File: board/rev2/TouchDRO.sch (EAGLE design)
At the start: 26 parts, among them U2 VREG_33, U3 VREG_5

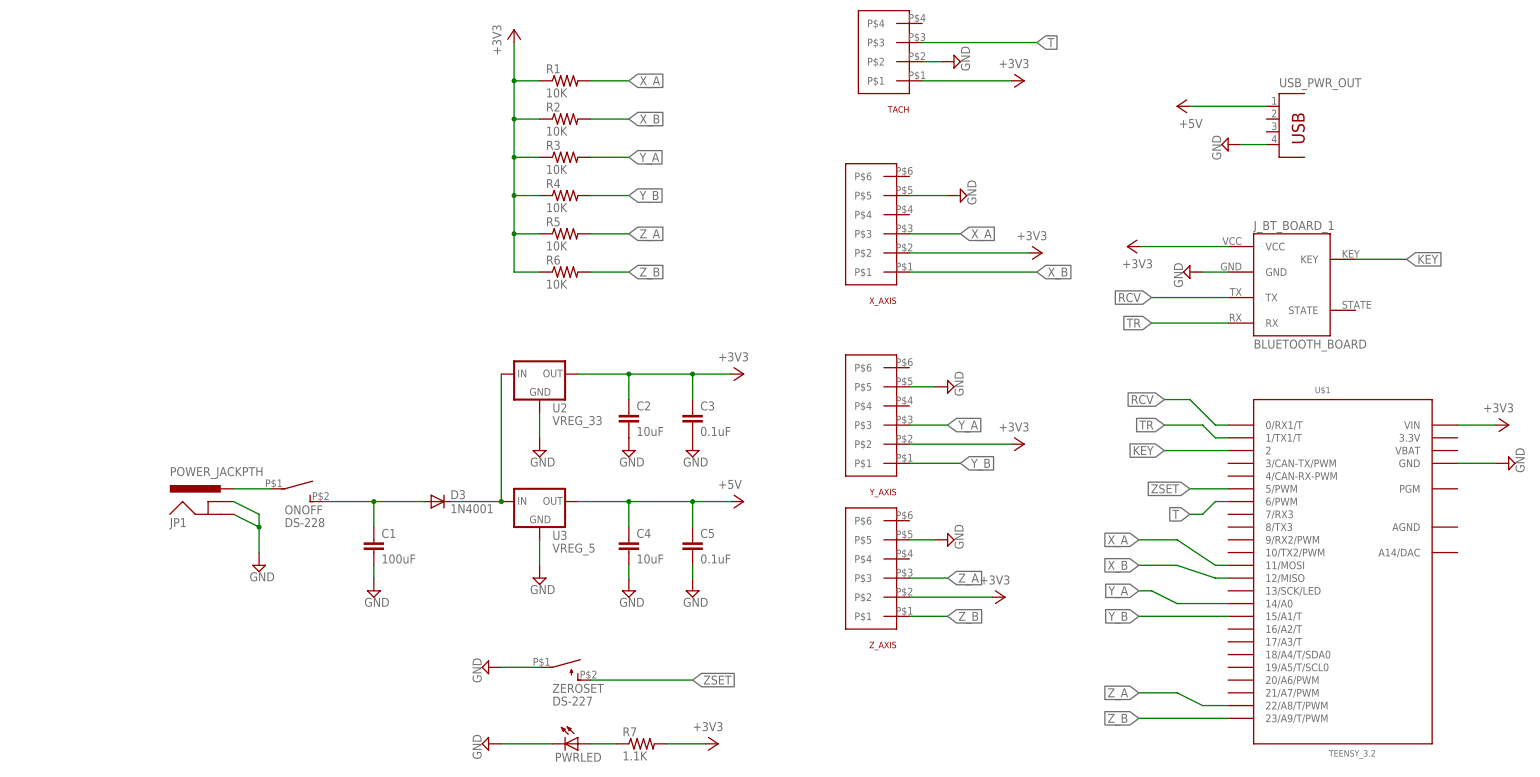
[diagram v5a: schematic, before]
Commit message: renamed connectors library. update regulators to have PWR signal pin. added Vcc resistor to support sherline encoder. updated TouchDRO sketch to use the new button and frequency libraries, disable bluetooth name set functionality
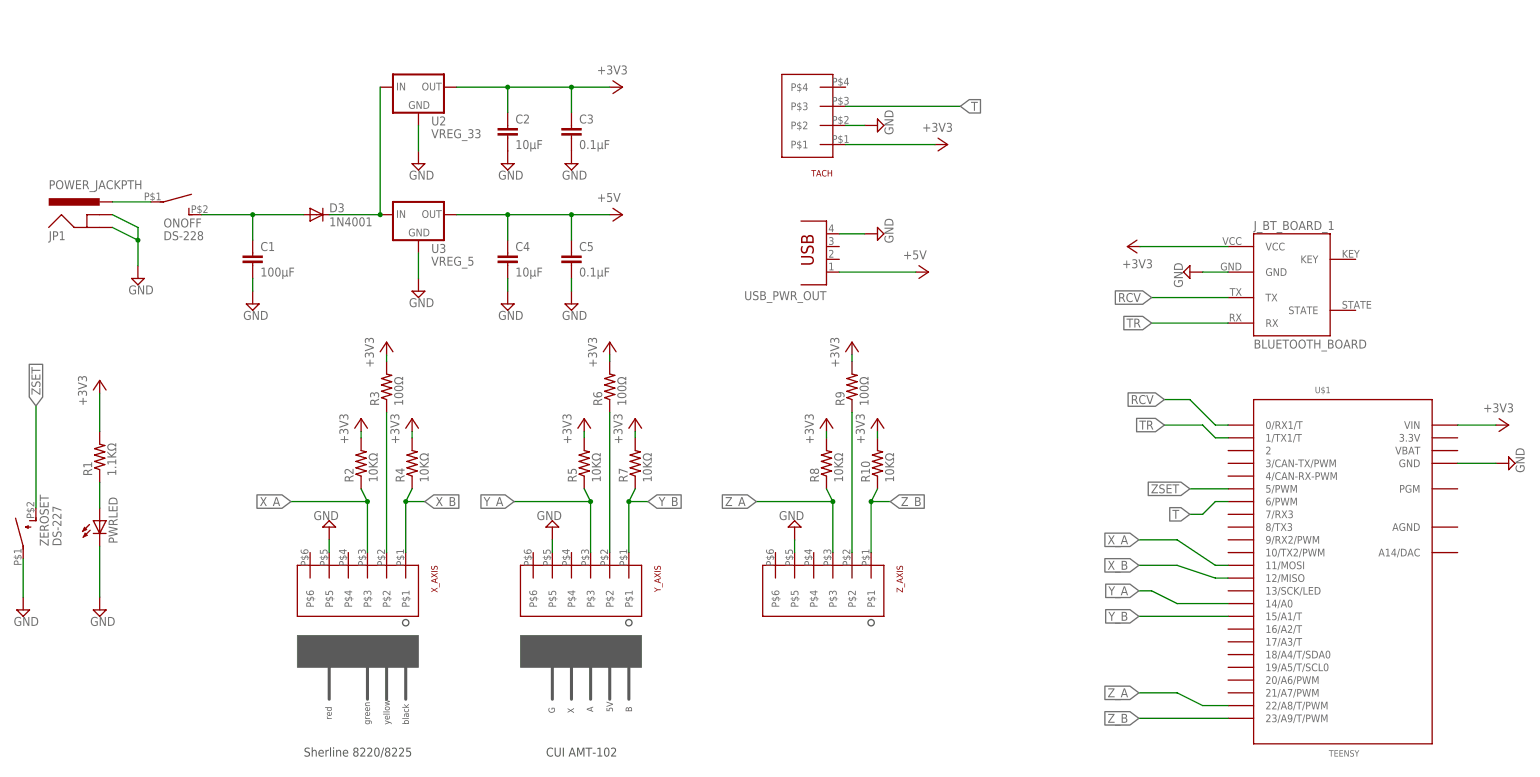
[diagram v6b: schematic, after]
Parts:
- added R10, R8: 10KΩ, SparkFun-Passives:RESISTOREZ
- added R9: 100Ω, SparkFun-Passives:RESISTOREZ
- C1: value 100uF -> 100µF
- C2, C4: value 10uF -> 10µF
- C3, C5: value 0.1uF -> 0.1µF
- R1: value 10K -> 1.1KΩ
- R2, R4, R5: value 10K -> 10KΩ
- R3, R6: value 10K -> 100Ω
- R7: value 1.1K -> 10KΩ
- U$1: value TEENSY_3.2 -> TEENSY
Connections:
- removed net KEY: J_BT_BOARD_1.KEY, U$1.2
- new net N$3: R9.1, Z_AXIS.P$2
- new net N$5: R6.1, Y_AXIS.P$2
- new net N$7: R3.1, X_AXIS.P$2
- net +3V3: now also R1.2, R10.2, R2.2, R3.2, R4.2, R5.2, R6.2, R8.2, R9.2; no longer R1.1, R2.1, R3.1, R4.1, R5.1, R6.1, X_AXIS.P$2, Y_AXIS.P$2, Z_AXIS.P$2
- net N$1: now also R1.1; no longer R7.1
- net X_A: now also R2.1; no longer R1.2
- net X_B: now also R4.1; no longer R2.2
- net Y_A: now also R5.1; no longer R3.2
- net Y_B: now also R7.1; no longer R4.2
- net Z_A: now also R8.1; no longer R5.2
- net Z_B: now also R10.1; no longer R6.2
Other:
- note added: "5V"
- note added: "A"
- note added: "B"
- note added: "CUI AMT-102"
- note added: "G"
- note added: "Sherline 8220/8225"
- note added: "X"
- note added: "black"
- note added: "green"
- note added: "red"
- note added: "yellow"
- moved on the sheet: C1, C2, C3, C4, C5, D3, JP1, ONOFF, PWRLED, R1, R2, R3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

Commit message: cleaned up connector components. updated images
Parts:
- renumbered U2 to VREG33, U3 to VREG50
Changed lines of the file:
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@@
 <setting verticaltext="up"/>
 </settings>
-<grid distance="0.05" unitdist="inch" unit="inch" style="lines" multiple="1" display="no" altdistance="0.025" altunitdist="inch" altunit="inch"/>
+<grid distance="0.1" unitdist="inch" unit="inch" style="lines" multiple="1" display="no" altdistance="0.01" altunitdist="inch" altunit="inch"/>
 <layers>
 <layer number="1" name="Top" color="4" fill="1" visible="no" active="no"/>
@@
 <part name="ZEROSET" library="Switches" deviceset="DS-227" device=""/>
 <part name="ONOFF" library="Switches" deviceset="DS-228" device=""/>
-<part name="U2" library="regulators" deviceset="VREG_33" device=""/>
-<part name="U3" library="regulators" deviceset="VREG_5" device=""/>
+<part name="VREG33" library="regulators" deviceset="VREG_33" device="" value="VREG_33"/>
+<part name="VREG50" library="regulators" deviceset="VREG_5" device="" value="VREG_5"/>
 <part name="PWRLED" library="led" deviceset="LED" device="3MM"/>
 <part name="SUPPLY4" library="supply2" deviceset="GND" device=""/>
@@
 <instance part="ZEROSET" gate="G$1" x="-184.15" y="-11.43"/>
 <instance part="ONOFF" gate="G$1" x="-153.67" y="54.61" rot="R270"/>
-<instance part="U2" gate="G$1" x="-105.41" y="77.47"/>
-<instance part="U3" gate="G$1" x="-105.41" y="52.07"/>
+<instance part="VREG33" gate="G$1" x="-105.41" y="77.47"/>
+<instance part="VREG50" gate="G$1" x="-105.41" y="52.07"/>
 <instance part="PWRLED" gate="G$1" x="-168.91" y="-8.89"/>
 <instance part="SUPPLY4" gate="GND" x="-168.91" y="-26.67"/>
@@
 <pinref part="SUPPLY15" gate="GND" pin="GND"/>
 <wire x1="-105.41" y1="69.85" x2="-105.41" y2="64.77" width="0.1524" layer="91"/>
-<pinref part="U2" gate="G$1" pin="GND"/>
+<pinref part="VREG33" gate="G$1" pin="GND"/>
 </segment>
 <segment>
 <pinref part="SUPPLY18" gate="GND" pin="GND"/>
 <wire x1="-105.41" y1="39.37" x2="-105.41" y2="44.45" width="0.1524" layer="91"/>
-<pinref part="U3" gate="G$1" pin="GND"/>
+<pinref part="VREG50" gate="G$1" pin="GND"/>
 </segment>
 <segment>
@@
 <wire x1="-74.93" y1="52.07" x2="-67.31" y2="52.07" width="0.1524" layer="91"/>
 <wire x1="-87.63" y1="52.07" x2="-87.63" y2="46.99" width="0.1524" layer="91"/>
-<pinref part="U3" gate="G$1" pin="OUT"/>
+<pinref part="VREG50" gate="G$1" pin="OUT"/>
 <pinref part="C5" gate="G$1" pin="1"/>
 <wire x1="-74.93" y1="46.99" x2="-74.93" y2="52.07" width="0.1524" layer="91"/>
@@
 <wire x1="-74.93" y1="77.47" x2="-67.31" y2="77.47" width="0.1524" layer="91"/>
 <wire x1="-87.63" y1="77.47" x2="-87.63" y2="72.39" width="0.1524" layer="91"/>
-<pinref part="U2" gate="G$1" pin="OUT"/>
+<pinref part="VREG33" gate="G$1" pin="OUT"/>
 <pinref part="C3" gate="G$1" pin="1"/>
 <wire x1="-74.93" y1="72.39" x2="-74.93" y2="77.47" width="0.1524" layer="91"/>
@@
 <wire x1="-123.19" y1="52.07" x2="-113.03" y2="52.07" width="0.1524" layer="91"/>
 <junction x="-113.03" y="52.07"/>
-<pinref part="U2" gate="G$1" pin="IN"/>
-<pinref part="U3" gate="G$1" pin="IN"/>
-</segment>
-</net>
+<pinref part="VREG33" gate="G$1" pin="IN"/>
+<pinref part="VREG50" gate="G$1" pin="IN"/>
+</segment>
+</net>

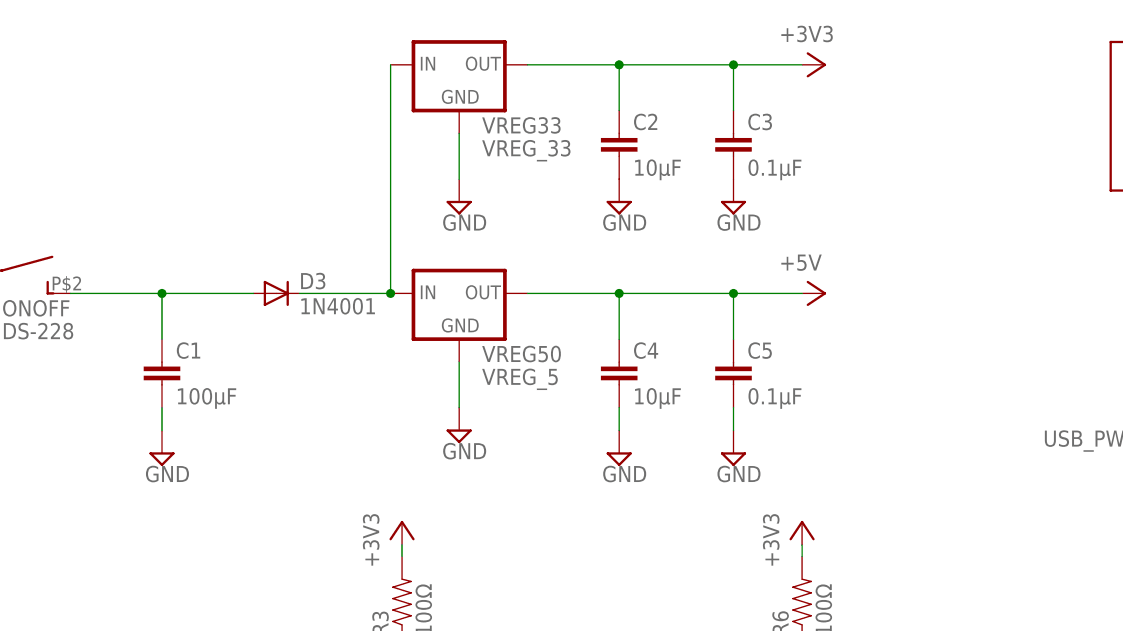
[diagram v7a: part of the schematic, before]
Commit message: adding latest pcb layout 3d model. finalized rev2 wiring, specifically wider routes on GND and VCC
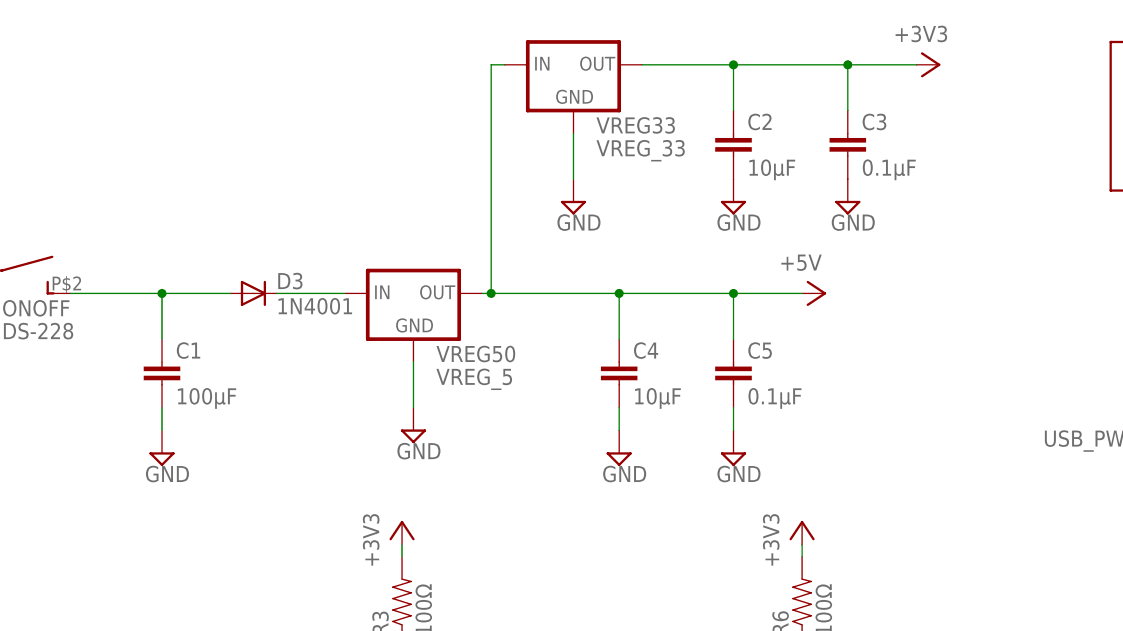
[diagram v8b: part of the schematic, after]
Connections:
- net +5V: now also VREG33.IN
- net D1: no longer VREG33.IN
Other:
- moved on the sheet: C2, C3, D3, VREG33, VREG50
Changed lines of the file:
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@@
 <instance part="SUPPLY10" gate="GND" x="-13.97" y="69.85" rot="R90"/>
 <instance part="SUPPLY11" gate="GND" x="48.26" y="40.64" rot="R270"/>
-<instance part="D3" gate="G$1" x="-125.73" y="52.07"/>
+<instance part="D3" gate="G$1" x="-128.27" y="52.07"/>
 <instance part="C4" gate="G$1" x="-87.63" y="41.91"/>
 <instance part="JP1" gate="G$1" x="-168.91" y="46.99"/>
 <instance part="SUPPLY13" gate="GND" x="-161.29" y="39.37"/>
-<instance part="SUPPLY15" gate="GND" x="-105.41" y="62.23"/>
+<instance part="SUPPLY15" gate="GND" x="-92.71" y="62.23"/>
 <instance part="SUPPLY16" gate="GND" x="-87.63" y="34.29"/>
-<instance part="SUPPLY18" gate="GND" x="-105.41" y="36.83"/>
+<instance part="SUPPLY18" gate="GND" x="-110.49" y="36.83"/>
 <instance part="SUPPLY20" gate="GND" x="-13.97" y="48.26" rot="R90"/>
 <instance part="P+2" gate="1" x="-64.77" y="52.07" rot="R270"/>
-<instance part="+3V3" gate="G$1" x="-64.77" y="77.47" rot="R270"/>
+<instance part="+3V3" gate="G$1" x="-52.07" y="77.47" rot="R270"/>
 <instance part="+3V4" gate="G$1" x="111.76" y="10.16" rot="R270"/>
 <instance part="+3V6" gate="G$1" x="0" y="66.04" rot="R270"/>
-<instance part="C2" gate="G$1" x="-87.63" y="67.31"/>
-<instance part="SUPPLY1" gate="GND" x="-87.63" y="62.23"/>
+<instance part="C2" gate="G$1" x="-74.93" y="67.31"/>
+<instance part="SUPPLY1" gate="GND" x="-74.93" y="62.23"/>
 <instance part="+3V1" gate="G$1" x="35.814" y="45.72" rot="R90"/>
 <instance part="P+1" gate="1" x="-3.81" y="40.64" rot="R270"/>
@@
 <instance part="ZEROSET" gate="G$1" x="-184.15" y="-11.43"/>
 <instance part="ONOFF" gate="G$1" x="-153.67" y="54.61" rot="R270"/>
-<instance part="VREG33" gate="G$1" x="-105.41" y="77.47"/>
-<instance part="VREG50" gate="G$1" x="-105.41" y="52.07"/>
+<instance part="VREG33" gate="G$1" x="-92.71" y="77.47"/>
+<instance part="VREG50" gate="G$1" x="-110.49" y="52.07"/>
 <instance part="PWRLED" gate="G$1" x="-168.91" y="-8.89"/>
 <instance part="SUPPLY4" gate="GND" x="-168.91" y="-26.67"/>
@@
 <instance part="C1" gate="G$1" x="-138.43" y="41.91"/>
 <instance part="SUPPLY8" gate="GND" x="-138.43" y="34.29"/>
-<instance part="C3" gate="G$1" x="-74.93" y="67.31"/>
-<instance part="SUPPLY9" gate="GND" x="-74.93" y="62.23"/>
+<instance part="C3" gate="G$1" x="-62.23" y="67.31"/>
+<instance part="SUPPLY9" gate="GND" x="-62.23" y="62.23"/>
 <instance part="C5" gate="G$1" x="-74.93" y="41.91"/>
 <instance part="SUPPLY12" gate="GND" x="-74.93" y="34.29"/>
@@
 <segment>
 <pinref part="SUPPLY15" gate="GND" pin="GND"/>
-<wire x1="-105.41" y1="69.85" x2="-105.41" y2="64.77" width="0.1524" layer="91"/>
+<wire x1="-92.71" y1="69.85" x2="-92.71" y2="64.77" width="0.1524" layer="91"/>
 <pinref part="VREG33" gate="G$1" pin="GND"/>
 </segment>
 <segment>
 <pinref part="SUPPLY18" gate="GND" pin="GND"/>
-<wire x1="-105.41" y1="39.37" x2="-105.41" y2="44.45" width="0.1524" layer="91"/>
+<wire x1="-110.49" y1="39.37" x2="-110.49" y2="44.45" width="0.1524" layer="91"/>
 <pinref part="VREG50" gate="G$1" pin="GND"/>
 </segment>
@@
 <pinref part="ONOFF" gate="G$1" pin="S"/>
 <pinref part="C1" gate="G$1" pin="1"/>
-<wire x1="-138.43" y1="52.07" x2="-128.27" y2="52.07" width="0.1524" layer="91"/>
+<wire x1="-138.43" y1="52.07" x2="-130.81" y2="52.07" width="0.1524" layer="91"/>
 <wire x1="-138.43" y1="46.99" x2="-138.43" y2="52.07" width="0.1524" layer="91"/>
 <junction x="-138.43" y="52.07"/>
@@
 <segment>
 <pinref part="P+2" gate="1" pin="+5V"/>
-<wire x1="-97.79" y1="52.07" x2="-87.63" y2="52.07" width="0.1524" layer="91"/>
+<wire x1="-102.87" y1="52.07" x2="-101.854" y2="52.07" width="0.1524" layer="91"/>
 <junction x="-87.63" y="52.07"/>
+<wire x1="-101.854" y1="52.07" x2="-87.63" y2="52.07" width="0.1524" layer="91"/>
 <wire x1="-87.63" y1="52.07" x2="-74.93" y2="52.07" width="0.1524" layer="91"/>
 <pinref part="C4" gate="G$1" pin="1"/>
@@
 <wire x1="-74.93" y1="46.99" x2="-74.93" y2="52.07" width="0.1524" layer="91"/>
 <junction x="-74.93" y="52.07"/>
+<pinref part="VREG33" gate="G$1" pin="IN"/>
+<wire x1="-100.33" y1="77.47" x2="-101.854" y2="77.47" width="0.1524" layer="91"/>
+<wire x1="-101.854" y1="77.47" x2="-101.854" y2="52.07" width="0.1524" layer="91"/>
+<junction x="-101.854" y="52.07"/>
 </segment>
 <segment>
@@
 <segment>
 <pinref part="+3V3" gate="G$1" pin="+3V3"/>
-<wire x1="-97.79" y1="77.47" x2="-87.63" y2="77.47" width="0.1524" layer="91"/>
-<junction x="-87.63" y="77.47"/>
-<wire x1="-87.63" y1="77.47" x2="-74.93" y2="77.47" width="0.1524" layer="91"/>
+<wire x1="-85.09" y1="77.47" x2="-74.93" y2="77.47" width="0.1524" layer="91"/>
+<junction x="-74.93" y="77.47"/>
+<wire x1="-74.93" y1="77.47" x2="-62.23" y2="77.47" width="0.1524" layer="91"/>
 <pinref part="C2" gate="G$1" pin="1"/>
-<wire x1="-74.93" y1="77.47" x2="-67.31" y2="77.47" width="0.1524" layer="91"/>
-<wire x1="-87.63" y1="77.47" x2="-87.63" y2="72.39" width="0.1524" layer="91"/>
+<wire x1="-62.23" y1="77.47" x2="-54.61" y2="77.47" width="0.1524" layer="91"/>
+<wire x1="-74.93" y1="77.47" x2="-74.93" y2="72.39" width="0.1524" layer="91"/>
 <pinref part="VREG33" gate="G$1" pin="OUT"/>
 <pinref part="C3" gate="G$1" pin="1"/>
-<wire x1="-74.93" y1="72.39" x2="-74.93" y2="77.47" width="0.1524" layer="91"/>
-<junction x="-74.93" y="77.47"/>
+<wire x1="-62.23" y1="72.39" x2="-62.23" y2="77.47" width="0.1524" layer="91"/>
+<junction x="-62.23" y="77.47"/>
 </segment>
 <segment>
@@
 <net name="D1" class="0">
 <segment>
-<wire x1="-113.03" y1="52.07" x2="-113.03" y2="77.47" width="0.1524" layer="91"/>
 <pinref part="D3" gate="G$1" pin="C"/>
-<wire x1="-123.19" y1="52.07" x2="-113.03" y2="52.07" width="0.1524" layer="91"/>
-<junction x="-113.03" y="52.07"/>
-<pinref part="VREG33" gate="G$1" pin="IN"/>
+<wire x1="-125.73" y1="52.07" x2="-118.11" y2="52.07" width="0.1524" layer="91"/>
 <pinref part="VREG50" gate="G$1" pin="IN"/>
 </segment>
